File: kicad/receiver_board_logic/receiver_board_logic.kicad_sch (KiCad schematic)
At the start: 8 parts, among them J2 Motor 1, J3 Motor 2, SW2 Pair/Direction, U4 Dual H Bridge, U5 ESP32-C3-SuperMini

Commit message: Update GPIO assignments and complete first-pass PCB layout
Swap motor control IN1/IN2 pins to simplify PCB routing:
- Motor 1: IN1 GPIO4, IN2 GPIO3 (was IN1 GPIO3, IN2 GPIO4)
- Motor 2: IN1 GPIO7, IN2 GPIO6 (was IN1 GPIO6, IN2 GPIO7)

Updated documentation:
- lib/hardware.py: Motor GPIO pin definitions
- README.md: Receiver GPIO assignment table
- receiver/README.md: Hardware pin descriptions

PCB design progress:
- Controller board: First-pass layout and routing complete
- Receiver logic board: First-pass layout and routing complete
- Receiver power board: First-pass layout and routing complete
- All decoupling capacitors added (470µF on TB6612 VM, 0.1µF on logic)
- Verified netlists: power, ground, GPIO, and board-to-board connections

Design notes:
- Potentiometer uses pin socket for off-board panel mount (bent legs)
- P-FET uses bent legs for mechanical positioning in enclosure
- P-FET on logic board near high-current loads (smart placement)
- Board-to-board connector properly routes all 6 signals

Co-Authored-By: Claude Sonnet 4.5 <noreply@anthropic.com>
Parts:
- added J1: B2B, Connector_PinSocket_2.54mm:PinSocket_1x06_P2.54mm_Vertical, symbol Connector:Conn_01x06_Socket
- added Q1: FQP27P06, Package_TO_SOT_THT:TO-220-3_Vertical, symbol Transistor_FET:FQP27P06
- added R1: 10k, Resistor_THT:R_Axial_DIN0207_L6.3mm_D2.5mm_P7.62mm_Horizontal, symbol Device:R
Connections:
- net GND: now also J1.3 (Pin_3)
- net LED_ESP: now also J1.6 (Pin_6)
- net MOT1_IN1: now also U5.4 (IO4); no longer U5.5 (IO3)
- net MOT1_IN2: now also U5.5 (IO3); no longer U5.4 (IO4)
- net MOT2_IN1: now also U5.14 (IO7); no longer U5.15 (IO6)
- net MOT2_IN2: now also U5.15 (IO6); no longer U5.14 (IO7)
- net 5V_BUCK renamed 5v_BUCK
- net 5v_BUCK: now also J1.5 (Pin_5)
- net 7V4_FET renamed 7v4_FET
- net 7v4_FET: now also J1.1 (Pin_1), Q1.2 (D)
- new net 7v4_BMS: J1.2 (Pin_2), Q1.3 (S), R1.1
- new net PWR_SW: J1.4 (Pin_4), Q1.1 (G), R1.2

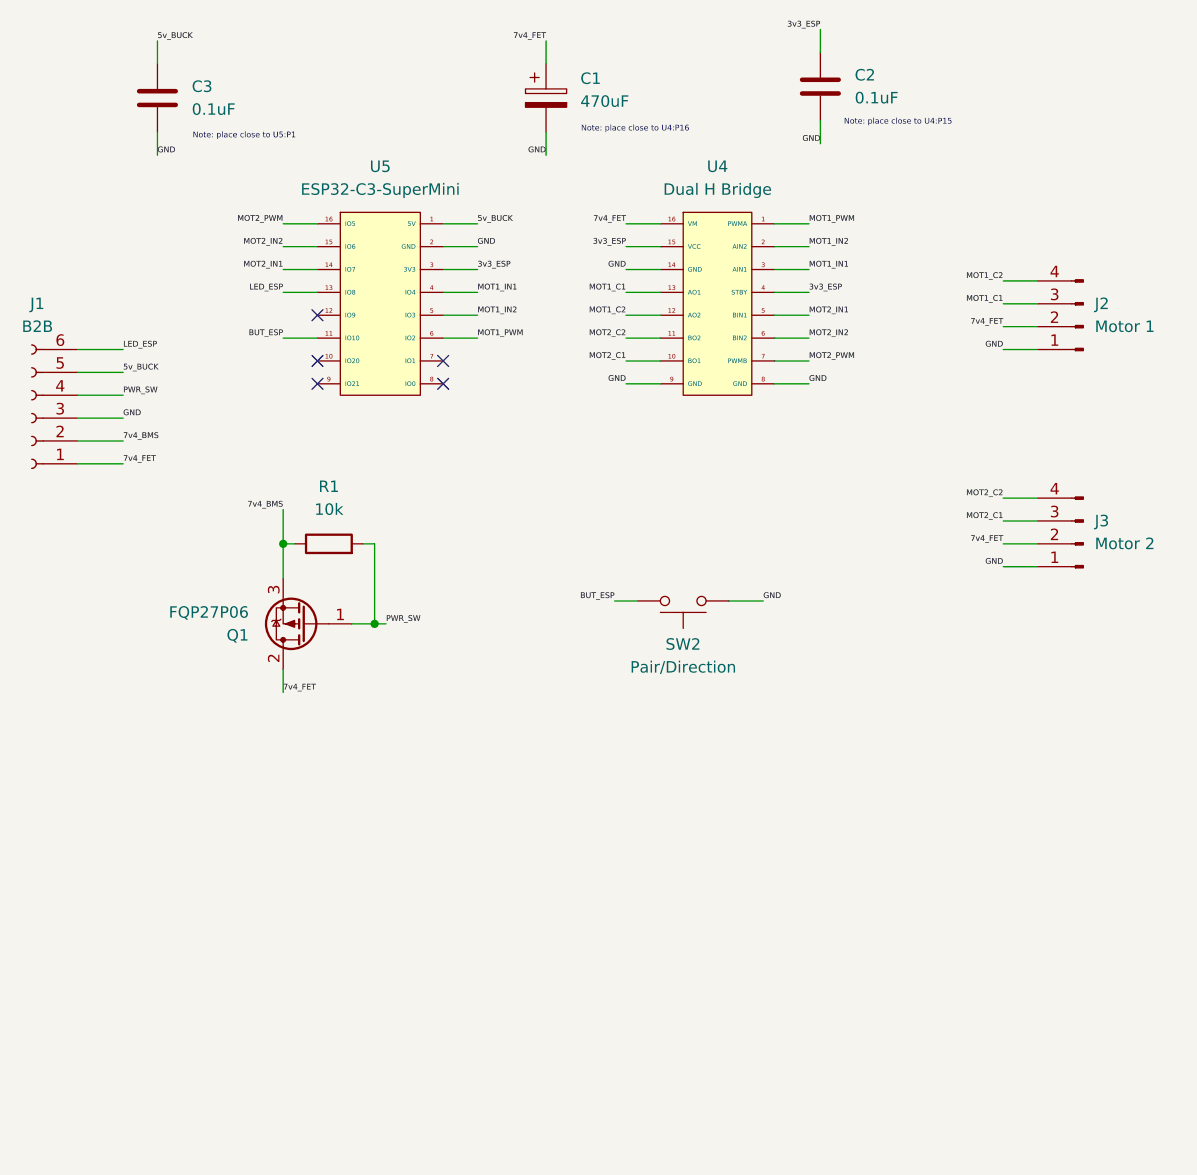
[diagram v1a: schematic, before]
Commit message: Remove BMS and reorganize receiver boards for external charging
Major schematic and layout revision based on EE review:

- Remove BMS from receiver design; pivot to external LiPo charging
- Reorganize components between power and logic boards:
  - Logic board: P-FET power switch, buck converter, UI (LED/button), debug UART
  - Power board: ESP32-C3, motor driver, battery monitoring
- Add voltage dividers for 2S LiPo monitoring (B+ and BM)
  - Safe ADC voltages: B+ = 2.36V max, BM = 2.47V max
- Add debug UART headers (GPIO20/21) for serial output when USB unavailable
- Fix P-FET drain connection to properly power both buck and motor system
- Update B2B connectors to dual 6-pin configuration (signal + power)
- Minor controller board PCB layout adjustments

Co-Authored-By: Claude Sonnet 4.5 <noreply@anthropic.com>
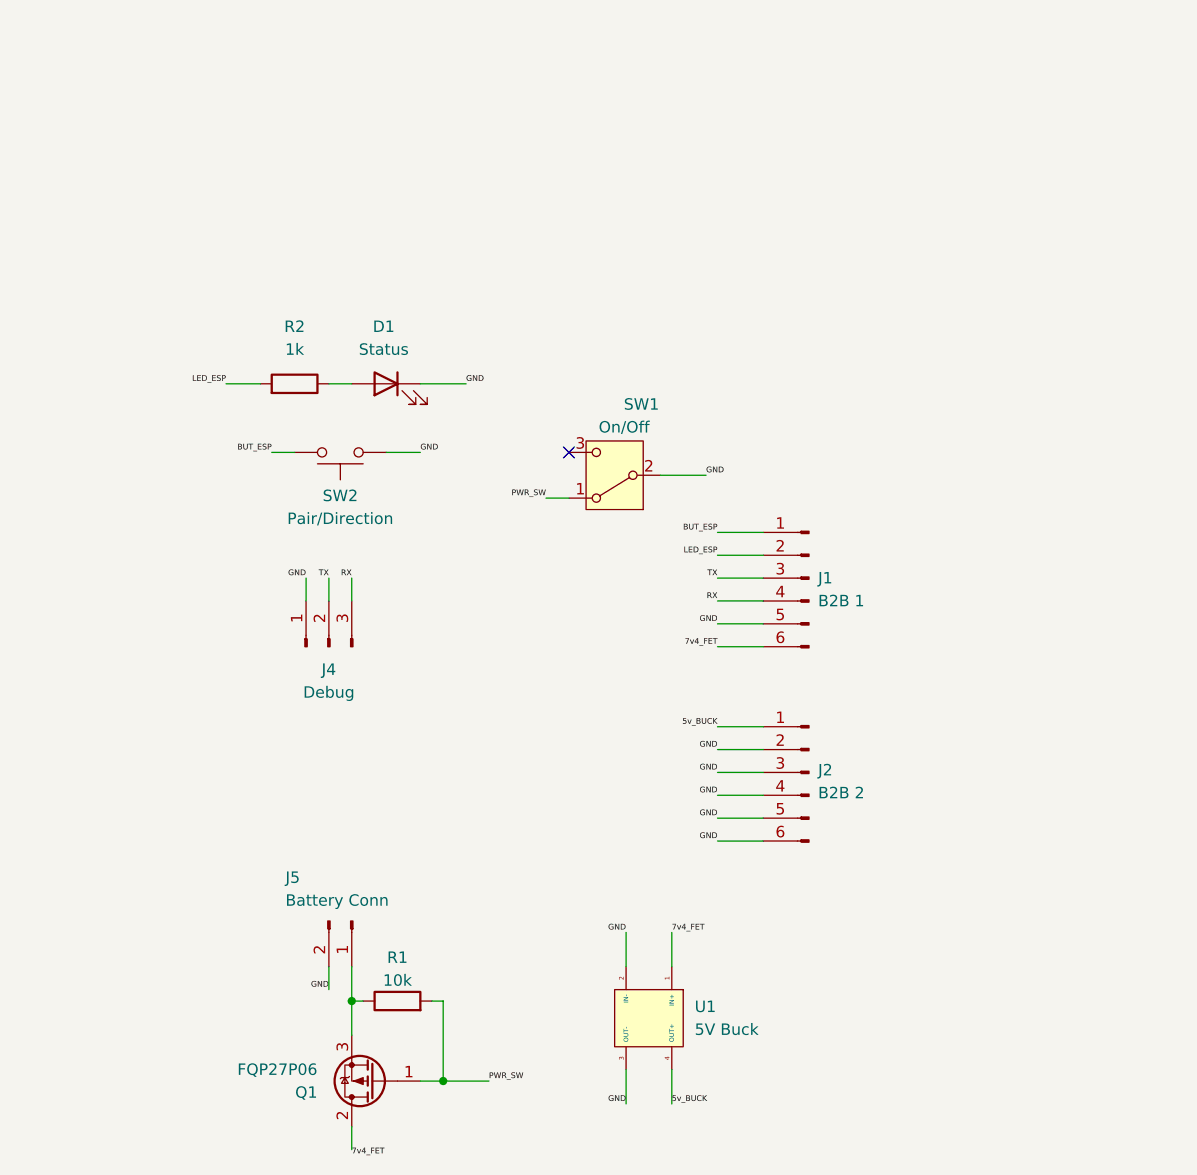
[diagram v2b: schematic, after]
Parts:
- removed C1: 470uF, Capacitor_THT:CP_Radial_D8.0mm_P5.00mm, symbol Device:C_Polarized
- removed C2, C3: 0.1uF, Capacitor_THT:C_Disc_D5.0mm_W2.5mm_P5.00mm, symbol Device:C
- removed J1: B2B, Connector_PinSocket_2.54mm:PinSocket_1x06_P2.54mm_Vertical, symbol Connector:Conn_01x06_Socket
- removed J2: Motor 1, Connector_JST:JST_XH_B4B-XH-A_1x04_P2.50mm_Vertical, symbol Connector:Conn_01x04_Pin
- removed J3: Motor 2, Connector_JST:JST_XH_B4B-XH-A_1x04_P2.50mm_Vertical, symbol Connector:Conn_01x04_Pin
- removed U4: Dual H Bridge, ESP32_Lego_PF:TB6612FNG, symbol ESP32_Lego_PF:TB6612FNG
- removed U5: ESP32-C3-SuperMini, ESP32_Lego_PF:ESP32-C3-SuperMini, symbol ESP32_Lego_PF:ESP32-C3-SuperMini
- added D1: Status, LED_THT:LED_D5.0mm, symbol Device:LED
- added J1: B2B 1, Connector_PinHeader_2.54mm:PinHeader_1x06_P2.54mm_Vertical, symbol Connector:Conn_01x06_Pin
- added J2: B2B 2, Connector_PinHeader_2.54mm:PinHeader_1x06_P2.54mm_Vertical, symbol Connector:Conn_01x06_Pin
- added J4: Debug, Connector_PinHeader_2.54mm:PinHeader_1x03_P2.54mm_Vertical, symbol Connector:Conn_01x03_Pin
- added J5: Battery Conn, Connector_PinHeader_2.54mm:PinHeader_1x02_P2.54mm_Vertical, symbol Connector:Conn_01x02_Pin
- added R2: 1k, Resistor_THT:R_Axial_DIN0207_L6.3mm_D2.5mm_P7.62mm_Horizontal, symbol Device:R
- added SW1: On/Off, ESP32_Lego_PF:Slide_Switch_SPDT_12D00G, symbol Switch:SW_SPDT
- added U1: 5V Buck, ESP32_Lego_PF:MP1584EN, symbol ESP32_Lego_PF:MP1584EN
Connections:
- net 5v_BUCK: now also J2.1 (Pin_1), U1.4 (OUT+)
- net 7v4_FET: now also J1.6 (Pin_6), U1.1 (IN+)
- net BUT_ESP: now also J1.1 (Pin_1)
- net GND: now also D1.1 (K), J1.5 (Pin_5), J2.2 (Pin_2), J2.3 (Pin_3), J2.4 (Pin_4), J2.5 (Pin_5), J2.6 (Pin_6), J4.1 (Pin_1), J5.2 (Pin_2), SW1.2 (B), U1.2 (IN-), U1.3 (OUT-)
- net LED_ESP: now also J1.2 (Pin_2), R2.2
- net PWR_SW: now also SW1.1 (A)
- net 7v4_BMS: no longer names the net of Q1.3 (S), R1.1
- net 7v4_BMS: now also J5.1 (Pin_1)
- new net: D1.2 (A), R2.1
- new net RX: J1.4 (Pin_4), J4.3 (Pin_3)
- new net TX: J1.3 (Pin_3), J4.2 (Pin_2)
- no-connect marks 5 -> 1
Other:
- note removed: "Note: place close to U4:P15"
- note removed: "Note: place close to U4:P16"
- note removed: "Note: place close to U5:P1"
- moved on the sheet: Q1, R1, SW2
